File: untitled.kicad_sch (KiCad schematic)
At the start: 24 parts, among them IC28 INA226AIDGSR, IC29 TPS25940ARVCR

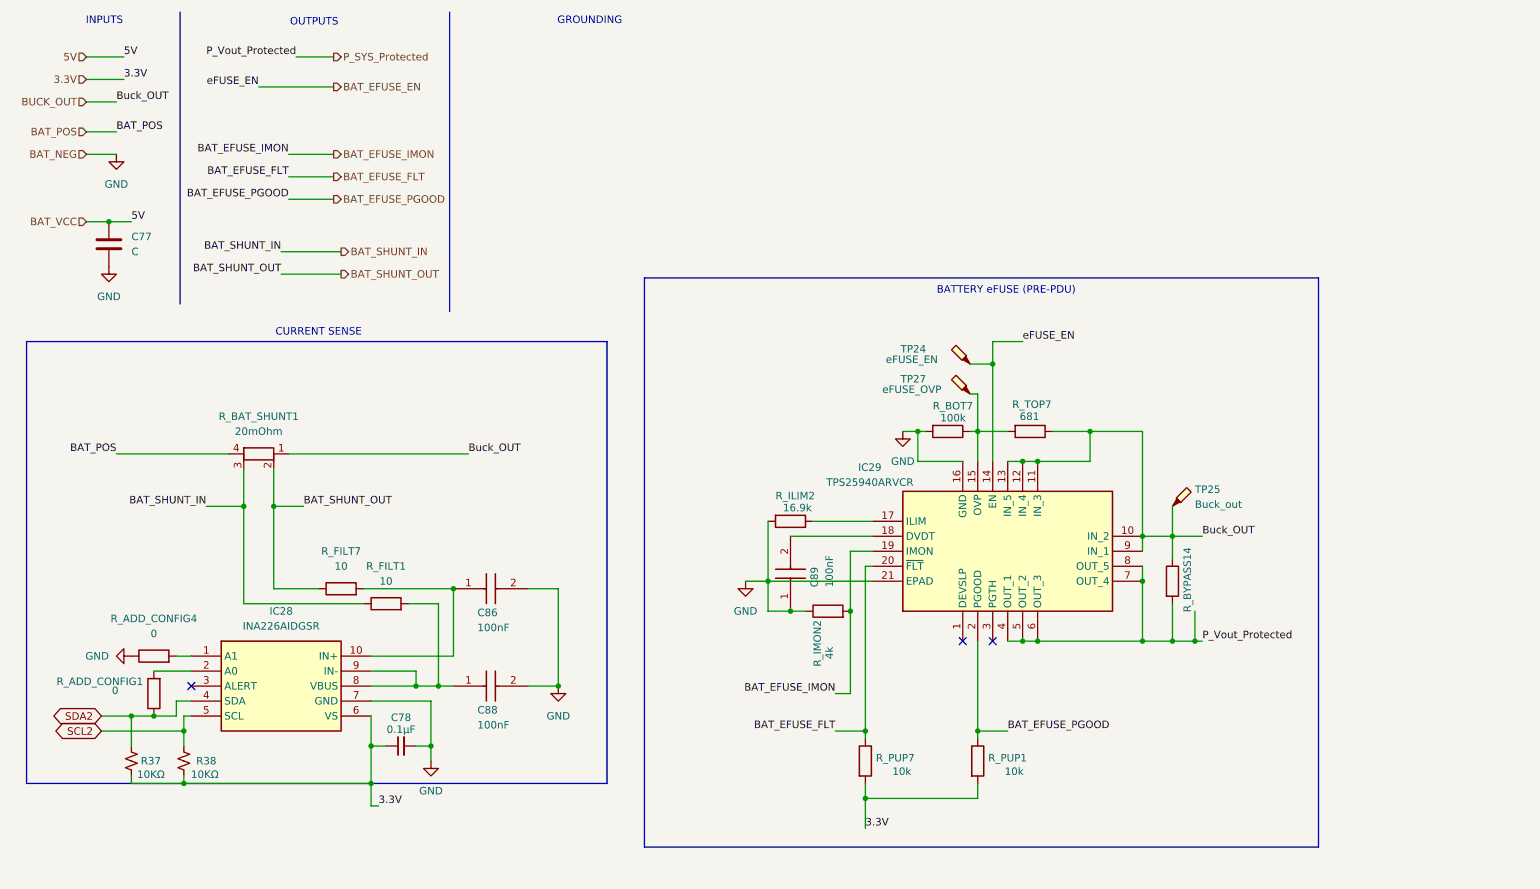
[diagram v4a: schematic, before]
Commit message: changed mcu power suppl
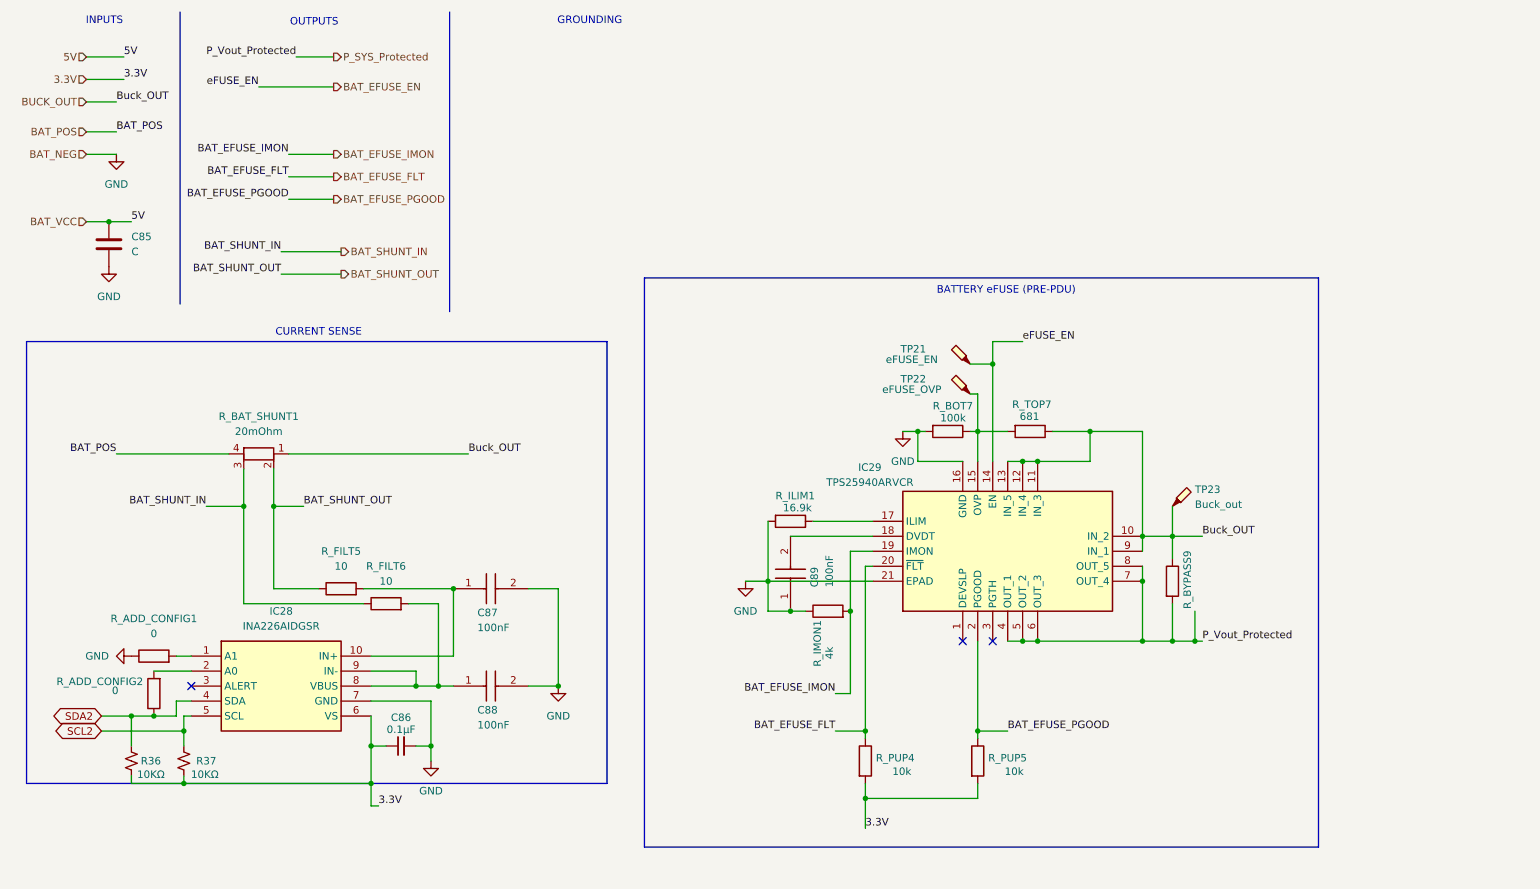
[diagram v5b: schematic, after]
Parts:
- renumbered C77 to C85, C78 to C86, C86 to C87, R37 to R36, R38 to R37, R_ADD_CONFIG4 to R_ADD_CONFIG1, R_ADD_CONFIG1 to R_ADD_CONFIG2, R_BYPASS14 to R_BYPASS9, R_FILT7 to R_FILT5, R_FILT1 to R_FILT6, R_ILIM2 to R_ILIM1, R_IMON2 to R_IMON1, R_PUP7 to R_PUP4, R_PUP1 to R_PUP5, TP24 to TP21, TP27 to TP22, TP25 to TP23
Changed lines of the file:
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@@
 		(dnp no)
 		(fields_autoplaced yes)
-		(property "Reference" "R_FILT1"
+		(property "Reference" "R_FILT6"
 			(at 80.01 107.95 90)
 			(effects
@@
 			(project "PULSE_ENG"
 				(path "/2de881bb-2e2a-47f9-96ed-b3393fa36b98/849a30d7-322f-4590-a198-8c58a018e511"
-					(reference "R_FILT1")
+					(reference "R_FILT6")
 					(unit 1)
 				)
@@
 		(on_board yes)
 		(dnp no)
-		(property "Reference" "C86"
+		(property "Reference" "C87"
 			(at 95.504 115.824 0)
 			(effects
@@
 			(project "PULSE_ENG"
 				(path "/2de881bb-2e2a-47f9-96ed-b3393fa36b98/849a30d7-322f-4590-a198-8c58a018e511"
-					(reference "C86")
+					(reference "C87")
 					(unit 1)
 				)
@@
 		(on_board yes)
 		(dnp no)
-		(property "Reference" "R_IMON2"
+		(property "Reference" "R_IMON1"
 			(at 153.162 124.968 0)
 			(effects
@@
 			(project "PULSE_ENG"
 				(path "/2de881bb-2e2a-47f9-96ed-b3393fa36b98/849a30d7-322f-4590-a198-8c58a018e511"
-					(reference "R_IMON2")
+					(reference "R_IMON1")
 					(unit 1)
 				)
@@
 		(on_board yes)
 		(dnp no)
-		(property "Reference" "R38"
+		(property "Reference" "R37"
 			(at 49.53 140.97 0)
 			(effects
@@
 			(project "PULSE_ENG"
 				(path "/2de881bb-2e2a-47f9-96ed-b3393fa36b98/849a30d7-322f-4590-a198-8c58a018e511"
-					(reference "R38")
+					(reference "R37")
 					(unit 1)
 				)
@@
 		(on_board yes)
 		(dnp no)
-		(property "Reference" "C78"
+		(property "Reference" "C86"
 			(at 82.55 133.604 90)
 			(effects
@@
 			(project "PULSE_ENG"
 				(path "/2de881bb-2e2a-47f9-96ed-b3393fa36b98/849a30d7-322f-4590-a198-8c58a018e511"
-					(reference "C78")
+					(reference "C86")
 					(unit 1)
 				)
@@
 		(on_board yes)
 		(dnp no)
-		(property "Reference" "R_PUP7"
+		(property "Reference" "R_PUP4"
 			(at 163.068 140.462 0)
 			(effects
@@
 			(project "PULSE_ENG"
 				(path "/2de881bb-2e2a-47f9-96ed-b3393fa36b98/849a30d7-322f-4590-a198-8c58a018e511"
-					(reference "R_PUP7")
+					(reference "R_PUP4")
 					(unit 1)
 				)
@@
 		(on_board yes)
 		(dnp no)
-		(property "Reference" "R_ADD_CONFIG1"
+		(property "Reference" "R_ADD_CONFIG2"
 			(at 24.13 127.508 0)
 			(effects
@@
 			(project "PULSE_ENG"
 				(path "/2de881bb-2e2a-47f9-96ed-b3393fa36b98/849a30d7-322f-4590-a198-8c58a018e511"
-					(reference "R_ADD_CONFIG1")
+					(reference "R_ADD_CONFIG2")
 					(unit 1)
 				)
@@
 		(dnp no)
 		(fields_autoplaced yes)
-		(property "Reference" "#PWR0136"
+		(property "Reference" "#PWR059"
 			(at 33.02 63.5 0)
 			(effects
@@
 			(project ""
 				(path "/2de881bb-2e2a-47f9-96ed-b3393fa36b98/849a30d7-322f-4590-a198-8c58a018e511"
-					(reference "#PWR0136")
+					(reference "#PWR059")
 					(unit 1)
 				)
@@
 		(dnp no)
 		(fields_autoplaced yes)
-		(property "Reference" "R_ADD_CONFIG4"
+		(property "Reference" "R_ADD_CONFIG1"
 			(at 40.64 116.84 90)
 			(effects
@@
 			(project "PULSE_ENG"
 				(path "/2de881bb-2e2a-47f9-96ed-b3393fa36b98/849a30d7-322f-4590-a198-8c58a018e511"
-					(reference "R_ADD_CONFIG4")
+					(reference "R_ADD_CONFIG1")
 					(unit 1)
 				)
@@
 		(dnp no)
 		(fields_autoplaced yes)
-		(property "Reference" "#PWR08"
+		(property "Reference" "#PWR063"
 			(at 109.22 134.62 0)
 			(effects
@@
 			(project "PULSE_ENG"
 				(path "/2de881bb-2e2a-47f9-96ed-b3393fa36b98/849a30d7-322f-4590-a198-8c58a018e511"
-					(reference "#PWR08")
+					(reference "#PWR063")
 					(unit 1)
 				)
@@
 		(dnp no)
 		(fields_autoplaced yes)
-		(property "Reference" "#PWR023"
+		(property "Reference" "#PWR065"
 			(at 167.64 91.44 0)
 			(effects
@@
 			(project "PULSE_ENG"
 				(path "/2de881bb-2e2a-47f9-96ed-b3393fa36b98/849a30d7-322f-4590-a198-8c58a018e511"
-					(reference "#PWR023")
+					(reference "#PWR065")
 					(unit 1)
 				)
@@
 		(dnp no)
 		(fields_autoplaced yes)
-		(property "Reference" "#PWR07"
+		(property "Reference" "#PWR062"
 			(at 87.63 147.32 0)
 			(effects
@@
 			(project "PULSE_ENG"
 				(path "/2de881bb-2e2a-47f9-96ed-b3393fa36b98/849a30d7-322f-4590-a198-8c58a018e511"
-					(reference "#PWR07")
+					(reference "#PWR062")
 					(unit 1)
 				)
@@
 		(dnp no)
 		(fields_autoplaced yes)
-		(property "Reference" "C77"
+		(property "Reference" "C85"
 			(at 36.83 52.0699 0)
 			(effects
@@
 			(project ""
 				(path "/2de881bb-2e2a-47f9-96ed-b3393fa36b98/849a30d7-322f-4590-a198-8c58a018e511"
-					(reference "C77")
+					(reference "C85")
 					(unit 1)
 				)
@@
 		(dnp no)
 		(fields_autoplaced yes)
-		(property "Reference" "#PWR027"
+		(property "Reference" "#PWR060"
 			(at 34.29 44.45 0)
 			(effects
@@
 			(project "PULSE_ENG"
 				(path "/2de881bb-2e2a-47f9-96ed-b3393fa36b98/849a30d7-322f-4590-a198-8c58a018e511"
-					(reference "#PWR027")
+					(reference "#PWR060")
 					(unit 1)
 				)
@@
 		(dnp no)
 		(fields_autoplaced yes)
-		(property "Reference" "#PWR013"
+		(property "Reference" "#PWR064"
 			(at 140.97 116.84 0)
 			(effects
@@
 			(project "PULSE_ENG"
 				(path "/2de881bb-2e2a-47f9-96ed-b3393fa36b98/849a30d7-322f-4590-a198-8c58a018e511"
-					(reference "#PWR013")
+					(reference "#PWR064")
 					(unit 1)
 				)
@@
 		(dnp no)
 		(fields_autoplaced yes)
-		(property "Reference" "R_FILT7"
+		(property "Reference" "R_FILT5"
 			(at 72.39 105.41 90)
 			(effects
@@
 			(project ""
 				(path "/2de881bb-2e2a-47f9-96ed-b3393fa36b98/849a30d7-322f-4590-a198-8c58a018e511"
-					(reference "R_FILT7")
+					(reference "R_FILT5")
 					(unit 1)
 				)
@@
 		(on_board yes)
 		(dnp no)
-		(property "Reference" "TP24"
+		(property "Reference" "TP21"
 			(at 169.418 71.12 90)
 			(effects
@@
 			(project ""
 				(path "/2de881bb-2e2a-47f9-96ed-b3393fa36b98/849a30d7-322f-4590-a198-8c58a018e511"
-					(reference "TP24")
+					(reference "TP21")
 					(unit 1)
 				)
@@
 		(dnp no)
 		(fields_autoplaced yes)
-		(property "Reference" "TP25"
+		(property "Reference" "TP23"
 			(at 217.17 94.9324 0)
 			(effects
@@
 			(project "PULSE_ENG"
 				(path "/2de881bb-2e2a-47f9-96ed-b3393fa36b98/849a30d7-322f-4590-a198-8c58a018e511"
-					(reference "TP25")
+					(reference "TP23")
 					(unit 1)
 				)
@@
 		(on_board yes)
 		(dnp no)
-		(property "Reference" "R_ILIM2"
+		(property "Reference" "R_ILIM1"
 			(at 146.05 96.012 90)
 			(effects
@@
 			(project "PULSE_ENG"
 				(path "/2de881bb-2e2a-47f9-96ed-b3393fa36b98/849a30d7-322f-4590-a198-8c58a018e511"
-					(reference "R_ILIM2")
+					(reference "R_ILIM1")
 					(unit 1)
 				)
@@
 		(on_board yes)
 		(dnp no)
-		(property "Reference" "R37"
+		(property "Reference" "R36"
 			(at 40.132 140.97 0)
 			(effects
@@
 			(project "PULSE_ENG"
 				(path "/2de881bb-2e2a-47f9-96ed-b3393fa36b98/849a30d7-322f-4590-a198-8c58a018e511"
-					(reference "R37")
+					(reference "R36")
 					(unit 1)
 				)
@@
 		(on_board yes)
 		(dnp no)
-		(property "Reference" "R_PUP1"
+		(property "Reference" "R_PUP5"
 			(at 182.118 140.462 0)
 			(effects
@@
 			(project "PULSE_ENG"
 				(path "/2de881bb-2e2a-47f9-96ed-b3393fa36b98/849a30d7-322f-4590-a198-8c58a018e511"
-					(reference "R_PUP1")
+					(reference "R_PUP5")
 					(unit 1)
 				)
@@
 		(dnp no)
 		(fields_autoplaced yes)
-		(property "Reference" "#PWR0135"
+		(property "Reference" "#PWR061"
 			(at 30.48 123.19 0)
 			(effects
@@
 			(project "PULSE_ENG"
 				(path "/2de881bb-2e2a-47f9-96ed-b3393fa36b98/849a30d7-322f-4590-a198-8c58a018e511"
-					(reference "#PWR0135")
+					(reference "#PWR061")
 					(unit 1)
 				)
@@
 		(on_board yes)
 		(dnp no)
-		(property "Reference" "TP27"
+		(property "Reference" "TP22"
 			(at 169.418 76.2 90)
 			(effects
@@
 			(project "PULSE_ENG"
 				(path "/2de881bb-2e2a-47f9-96ed-b3393fa36b98/849a30d7-322f-4590-a198-8c58a018e511"
-					(reference "TP27")
+					(reference "TP22")
 					(unit 1)
 				)
@@
 		(on_board yes)
 		(dnp no)
-		(property "Reference" "R_BYPASS14"
+		(property "Reference" "R_BYPASS9"
 			(at 215.9 110.236 90)
 			(effects
@@
 			(project "PULSE_ENG"
 				(path "/2de881bb-2e2a-47f9-96ed-b3393fa36b98/849a30d7-322f-4590-a198-8c58a018e511"
-					(reference "R_BYPASS14")
-					(unit 1)
-				)
+					(reference "R_BYPASS9")
+					(unit 1)
+				)
